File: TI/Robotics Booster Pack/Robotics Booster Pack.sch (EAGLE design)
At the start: 119 parts, among them U1 DRV8800, U10 74LVTH125.RGY, U11 SCHA4B0400, U12 BLUETOOTH-RN41", U13 XBEE-1XBEE-1_LOCK, U14 FDMA1024NZ, U2 DRV8800, U3 DRV8800, U4 DRV8800, U5 TPS5331[8/9].DQP, U6 TPS62082.DSG, U7 PCA9557.RGV, U8 MPU-6050, U9 INA220.DGS

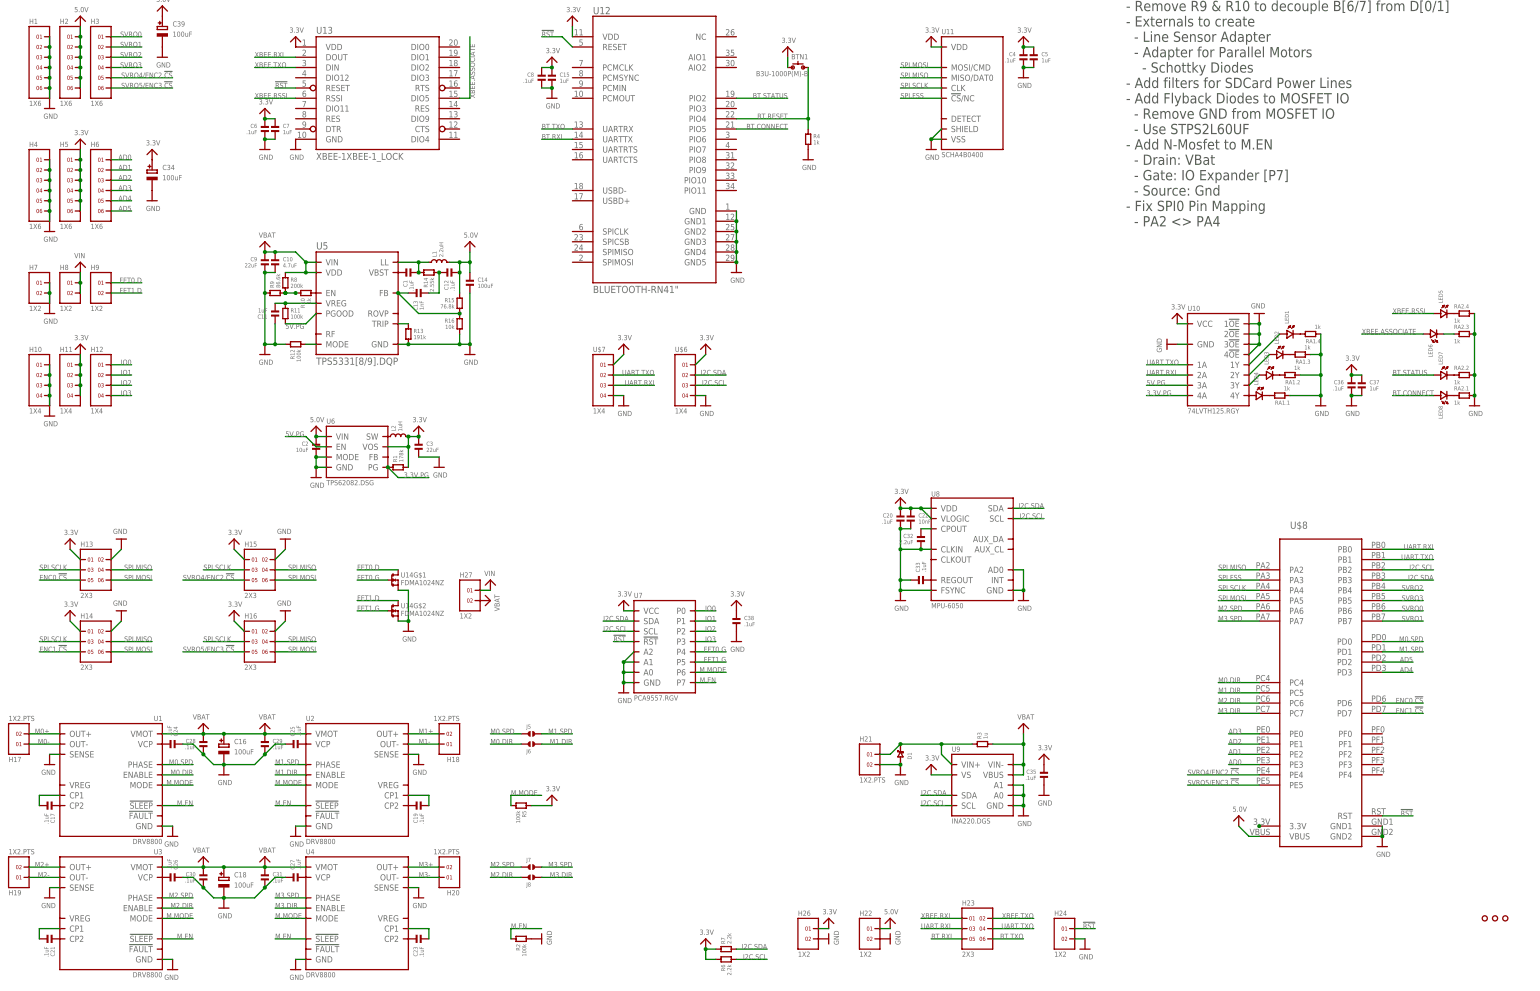
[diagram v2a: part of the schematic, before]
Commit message: Addressed all issues in github repo Moved GPIO & Mosfet connections up because of USB connector in Launchpad Fixed SPI pin swap Added diode between 5v and VBUS Changed jumpers for UART BT/XBee selection to SMD Jumpers
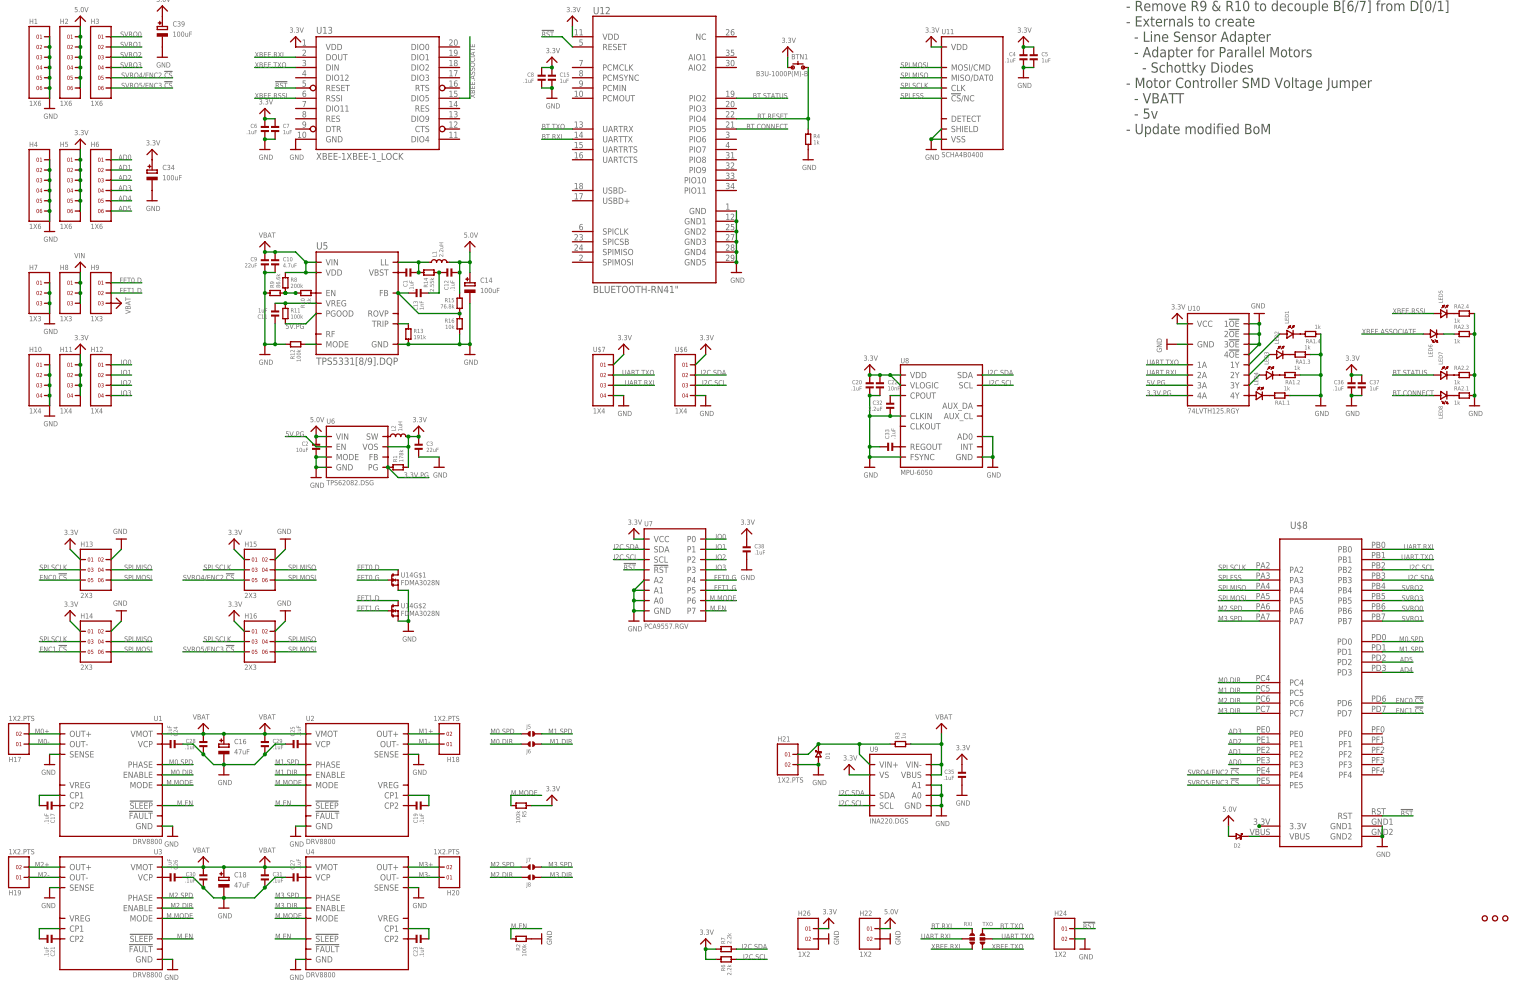
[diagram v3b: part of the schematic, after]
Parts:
- removed H23: 2X3, headers(2mm):2X3
- removed H27: 1X2, headers(.1in):1X2
- added D2: (no value), nxp:DIODE[SCHOTKY]-SOD123W
- added RXI, TXO: (no value), solderjumper:SOLDERJUMPER.3.LRG
- C14: device standardparts:CAPACITOR.1210 -> microbuilder:CAP_ELECTROLYTICPANASONIC_C
- C16, C18: value 100uF -> 47uF
- H7, H8, H9: value 1X2 -> 1X3; device headers(.1in):1X2 -> headers(.1in):1X3
- U14: value FDMA1024NZ -> FDMA3028N
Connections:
- new net N$16: D2.2, U$8.VBUS
- net 5.0V: now also C14.+, D2.1; no longer C14.1, U$8.VBUS
- net BT.RXI: now also RXI.1; no longer H23.5
- net BT.TXO: now also TXO.1; no longer H23.6
- net GND: now also C14.-, H7.3; no longer C14.2
- net SPI.MISO: now also U$8.PA4; no longer U$8.PA2
- net SPI.SCLK: now also U$8.PA2; no longer U$8.PA4
- net UART.RXI: now also RXI.2; no longer H23.3
- net UART.TXO: now also TXO.2; no longer H23.4
- net VBAT: now also H9.3; no longer H27.2
- net VIN: now also H8.3; no longer H27.1
- net XBEE.RXI: now also RXI.3; no longer H23.1
- net XBEE.TXO: now also TXO.3; no longer H23.2
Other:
- note added: "NOTES: - Remove R9 & R10 to decouple B[6/7] from D[0/1] - Externals to create - Line Sensor Adapter - Adapter for Parallel Motors - Schottky Diodes - Motor Controller SMD Voltage Jumper - VBATT - 5v - Update modified BoM"
- note removed: "NOTES: - Remove R9 & R10 to decouple B[6/7] from D[0/1] - Externals to create - Line Sensor Adapter - Adapter for Parallel Motors - Schottky Diodes - Add filters for SDCard Power Lines - Add Flyback Diodes to MOSFET IO - Remove GND from MOSFET IO - Use STPS2L60UF - Add N-Mosfet to M.EN - Drain: VBat - Gate: IO Expander [P7] - Source: Gnd - Fix SPI0 Pin Mapping - PA2 <> PA4"
- moved on the sheet: C20, C22, C32, C33, C35, C38, D1, H21, R3, U7, U8, U9

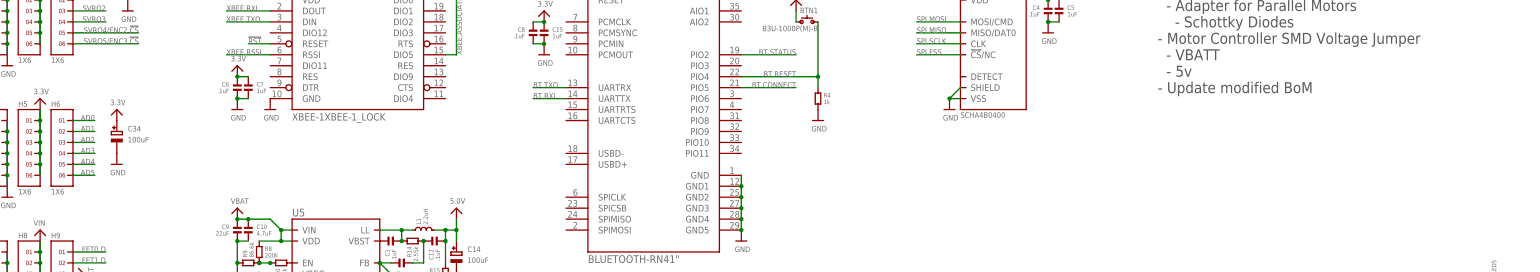
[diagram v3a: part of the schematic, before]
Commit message: Created AS5035 FLoating Encoder
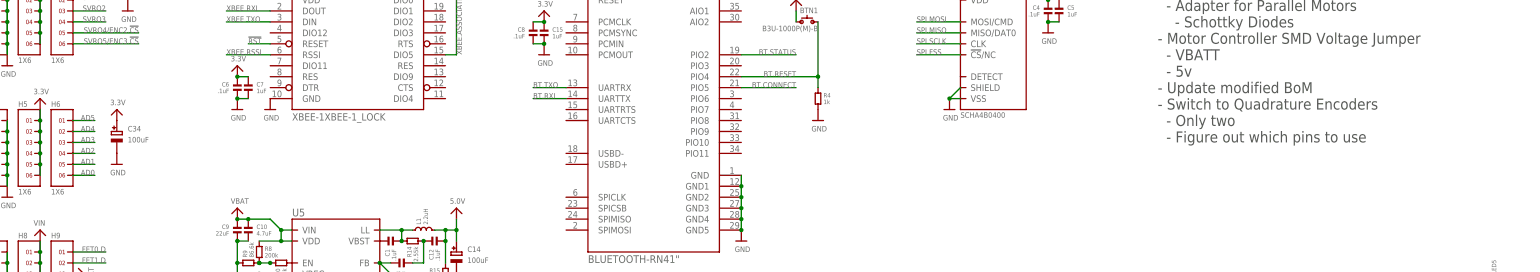
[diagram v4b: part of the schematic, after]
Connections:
- net AD0: now also H6.6; no longer H6.1
- net AD1: now also H6.5; no longer H6.2
- net AD2: now also H6.4; no longer H6.3
- net AD3: now also H6.3; no longer H6.4
- net AD4: now also H6.2; no longer H6.5
- net AD5: now also H6.1; no longer H6.6
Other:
- note added: "NOTES: - Remove R9 & R10 to decouple B[6/7] from D[0/1] - Externals to create - Line Sensor Adapter - Adapter for Parallel Motors - Schottky Diodes - Motor Controller SMD Voltage Jumper - VBATT - 5v - Update modified BoM - Switch to Quadrature Encoders - Only two - Figure out which pins to use"
- note removed: "NOTES: - Remove R9 & R10 to decouple B[6/7] from D[0/1] - Externals to create - Line Sensor Adapter - Adapter for Parallel Motors - Schottky Diodes - Motor Controller SMD Voltage Jumper - VBATT - 5v - Update modified BoM"

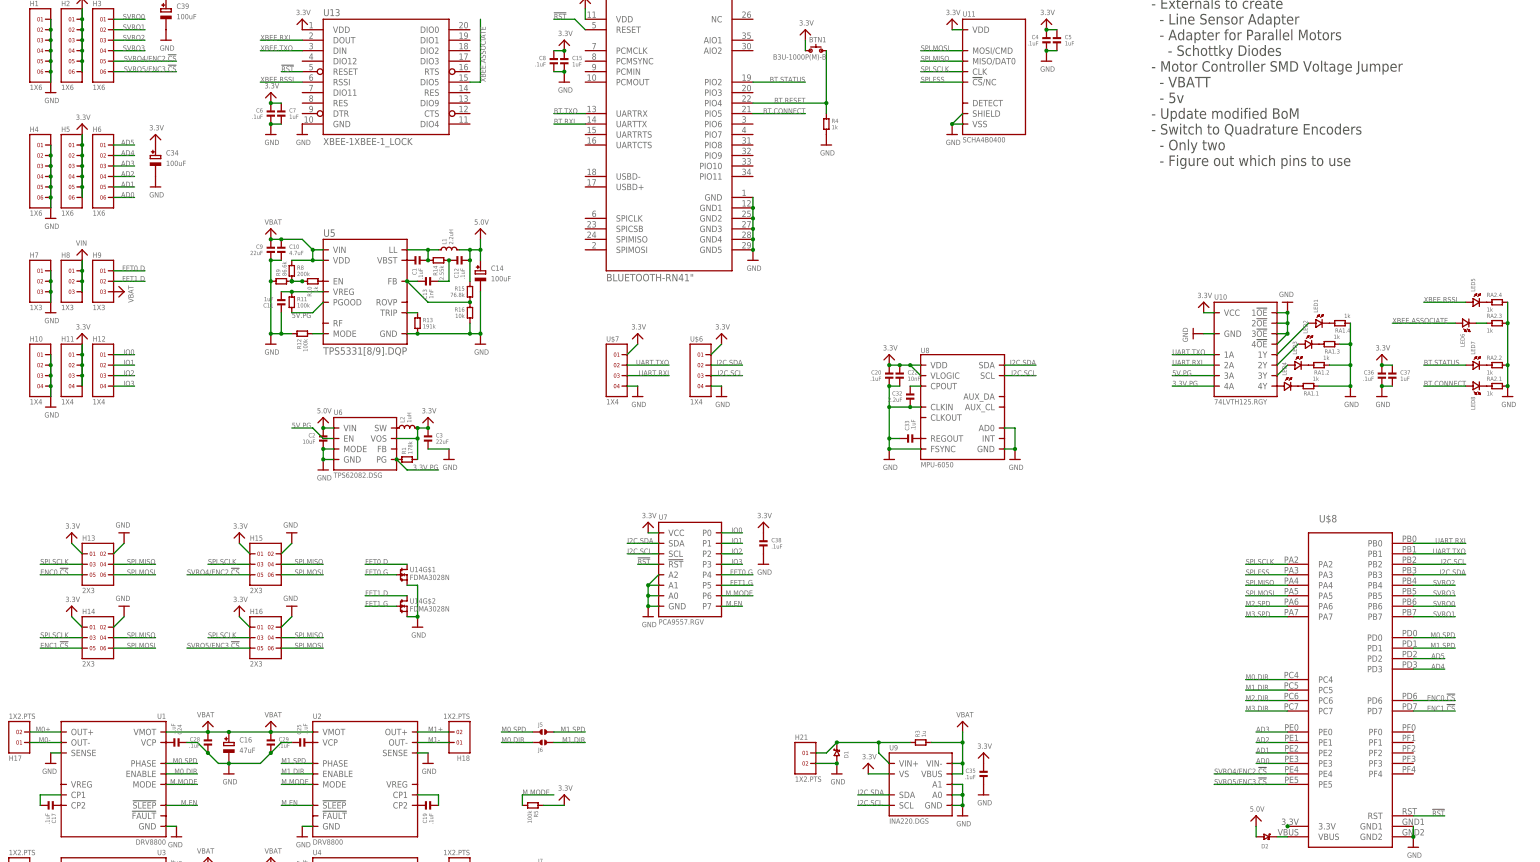
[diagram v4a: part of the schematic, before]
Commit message: Changed Pinouts of BoosterPack * SPI Encoders replaced with QEI * SD Card/SPI interface moved to port F * Motor Control Signals moved to port A
Layout still needs to be redone...
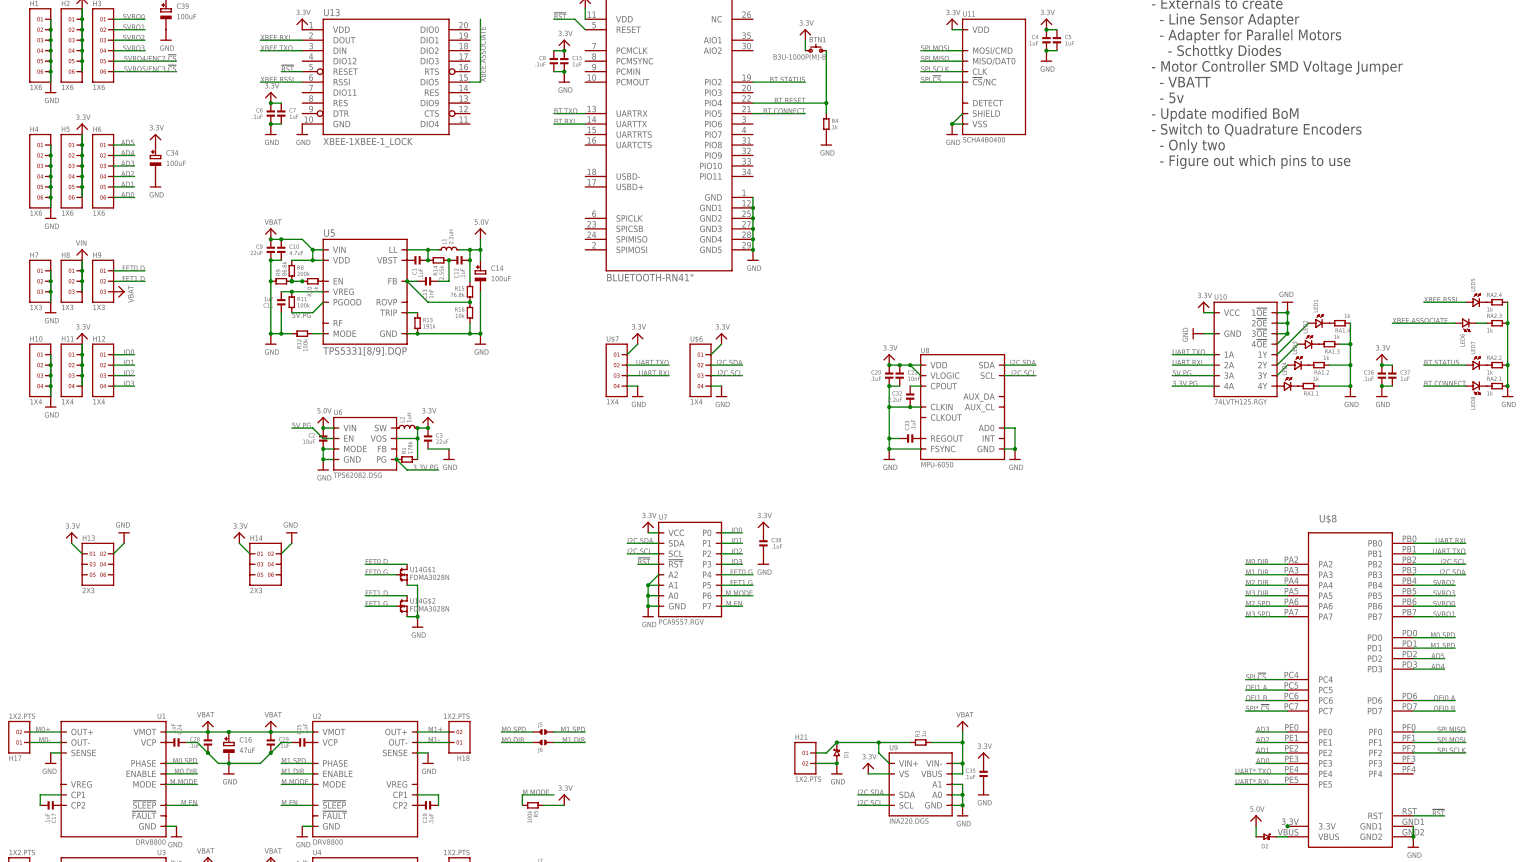
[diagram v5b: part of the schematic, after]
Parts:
- removed H15, H16: 2X3, headers(.1in):2X3
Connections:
- removed net ENC0.!CS: H13.5, U$8.PD6
- removed net ENC1.!CS: H14.5, U$8.PD7
- removed net SPI.FSS: U$8.PA3, U11.!CS!/NC
- new net QEI0.A: U$8.PD6
- new net QEI0.B: U$8.PD7
- new net QEI1.A: U$8.PC5
- new net QEI1.B: U$8.PC6
- new net SPI*.!CS: U$8.PC7
- new net SPI.!CS: U$8.PC4, U11.!CS!/NC
- new net UART*.RXI: U$8.PE5
- new net UART*.TXO: U$8.PE4
- net 3.3V: no longer H15.1, H16.1
- net GND: no longer H15.2, H16.2
- net M0.DIR: now also U$8.PA2; no longer U$8.PC4
- net M1.DIR: now also U$8.PA3; no longer U$8.PC5
- net M2.DIR: now also U$8.PA4; no longer U$8.PC6
- net M3.DIR: now also U$8.PA5; no longer U$8.PC7
- net SPI.MISO: now also U$8.PF0; no longer H13.4, H14.4, H15.4, H16.4, U$8.PA4
- net SPI.MOSI: now also U$8.PF1; no longer H13.6, H14.6, H15.6, H16.6, U$8.PA5
- net SPI.SCLK: now also U$8.PF2; no longer H13.3, H14.3, H15.3, H16.3, U$8.PA2
- net SVRO4/ENC2.!CS: no longer H15.5, U$8.PE4
- net SVRO5/ENC3.!CS: no longer H16.5, U$8.PE5
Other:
- moved on the sheet: H14

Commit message: Started routing v2. And by started, I mean rerouting _everything_
... The heck's wrong with me ...
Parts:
- removed BTN1: B3U-1000P(M)-B, omron:SPST.B3U-1000P(M)-B
- removed U$6, U$7: 1X4, headers(.1in):1X4
- added J2: (no value), solderjumper:SOLDERJUMPER.2.MED
- added U$9: 2X4, headers(.1in):2X4
- C14, C16, C18, C34, C39: device microbuilder:CAP_ELECTROLYTICPANASONIC_C -> microbuilder:CAP_ELECTROLYTICPANASONIC_D
- R2, R5: value 100k -> 10k
- RXI, TXO: device solderjumper:SOLDERJUMPER.3.LRG -> solderjumper:SOLDERJUMPER.3.LRG.12
- renumbered U$11 to U$14
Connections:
- removed net N$43: LED2.1, U10.2Y
- removed net N$51: LED1.2, RA1.4.2
- removed net N$52: LED2.2, RA1.3.2
- removed net N$6 (its old number): LED1.1, U10.1Y
- removed net SPI*.!CS: U$8.PC7
- removed net SVRO4/ENC2.!CS: H3.5
- removed net SVRO5/ENC3.!CS: H3.6
- removed net UART*.RXI: U$8.PE5
- removed net UART*.TXO: U$8.PE4
- new net N$26: LED2.2, U10.2Y
- new net N$28: LED1.2, U10.1Y
- new net N$30: LED1.1, RA1.4.2
- new net N$31: LED2.1, RA1.3.2
- new net SVRO4: H3.5, U$8.PE4
- new net SVRO5: H3.6, U$8.PE5
- net 3.3V: now also H13.3, H14.3, J2.2, U$9.1, U$9.2; no longer BTN1.2, H13.1, H14.1, U$6.1, U$7.1
- net 5.0V: no longer C2.1, U6.VIN
- net BT.RESET: now also J2.1; no longer BTN1.1
- net GND: now also H13.1, H14.1, U$9.7, U$9.8; no longer H13.2, H14.2, U$6.4, U$7.4
- net I2C.SCL: now also U$9.5, U$9.6; no longer U$6.3
- net I2C.SDA: now also U$9.3, U$9.4; no longer U$6.2
- net M.MODE: no longer U7.P6
- net M0.DIR: now also U$8.PC4; no longer U$8.PA2
- net M1.DIR: now also U$8.PC7; no longer U$8.PA3
- net M2.DIR: now also U$8.PF0; no longer U$8.PA4
- net M3.DIR: now also U$8.PF4; no longer U$8.PA5
- net N$16: now also H8.1, H8.2, H8.3; no longer D2.2, U$8.VBUS
- net QEI0.A: now also H13.5
- net QEI0.B: now also H13.6
- net QEI1.A: now also H14.5
- net QEI1.B: now also H14.6
- net SPI.!CS: now also U$8.PA3; no longer U$8.PC4
- net SPI.MISO: now also U$8.PA4; no longer U$8.PF0
- net SPI.MOSI: now also U$8.PA5; no longer U$8.PF1
- net SPI.SCLK: now also U$8.PA2; no longer U$8.PF2
- net UART.RXI: no longer U$7.3
- net UART.TXO: no longer U$7.2
- net VIN: now also C2.1, D2.2, U$8.VBUS, U6.VIN; no longer H8.1, H8.2, H8.3
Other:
- note added: "NOTES: - Move I2C and UART 50mil to left - Connect BT.RESET to IO Expander"
- note removed: "NOTES: - Remove R9 & R10 to decouple B[6/7] from D[0/1] - Externals to create - Line Sensor Adapter - Adapter for Parallel Motors - Schottky Diodes - Motor Controller SMD Voltage Jumper - VBATT - 5v - Update modified BoM - Switch to Quadrature Encoders - Only two - Figure out which pins to use"
- moved on the sheet: C1, C10, C11, C12, C13, C14, C38, C9, D2, L1, LED1, LED2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
